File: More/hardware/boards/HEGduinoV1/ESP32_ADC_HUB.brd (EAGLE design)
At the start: 71.9 x 30 mm, 8 parts

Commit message: Added some sensor designs, moved some stuff
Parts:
- moved ADS1115 1.27 mm to (40.0, 38.5)
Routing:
- net ADC_GND: track 44.0 -> 45.4 mm
- net SDA: track 36.6 -> 37.9 mm
- net VBAT: track 89.8 -> 88.7 mm
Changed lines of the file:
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@@
 <attribute name="VALUE" x="55.047590625" y="28.01005" size="0.4064" layer="27" ratio="10" rot="R180"/>
 </element>
-<element name="ADS1115" library="microbuilder" package="1X10_ROUND70" value="" x="40.040815625" y="37.223853125" smashed="yes" rot="R180">
-<attribute name="NAME" x="27.298803125" y="39.482015625" size="0.8128" layer="26" ratio="10" rot="MR270"/>
-<attribute name="VALUE" x="52.740815625" y="40.398853125" size="0.8128" layer="27" rot="R180"/>
+<element name="ADS1115" library="microbuilder" package="1X10_ROUND70" value="" x="40.040815625" y="38.493853125" smashed="yes" rot="R180">
+<attribute name="NAME" x="27.298803125" y="40.752015625" size="0.8128" layer="26" ratio="10" rot="MR270"/>
+<attribute name="VALUE" x="52.740815625" y="41.668853125" size="0.8128" layer="27" rot="R180"/>
 </element>
 <element name="R1" library="resistor" library_urn="urn:adsk.eagle:library:348" package="0204/7" package3d_urn="urn:adsk.eagle:package:23498/1" value="" x="54.3327375" y="36.29111875" smashed="yes" rot="R270">
@@
 </signal>
 <signal name="VBAT">
-<wire x1="51.435" y1="40.005" x2="51.435" y2="37.1475" width="0.254" layer="1"/>
+<wire x1="51.435" y1="40.005" x2="51.435" y2="38.25875" width="0.254" layer="1"/>
 <wire x1="51.435" y1="40.005" x2="56.8325" y2="40.005" width="0.254" layer="1"/>
 <wire x1="51.435" y1="40.005" x2="19.52625" y2="40.005" width="0.254" layer="1"/>
@@
 <wire x1="50.165" y1="32.54375" x2="50.165" y2="41.43375" width="0.254" layer="16"/>
 <wire x1="50.165" y1="41.43375" x2="53.81625" y2="45.085" width="0.254" layer="16"/>
-<wire x1="43.815" y1="37.1475" x2="43.815" y2="32.54375" width="0.254" layer="16"/>
+<wire x1="43.815" y1="38.4175" x2="43.815" y2="32.54375" width="0.254" layer="16"/>
 <via x="43.815" y="32.54375" extent="1-16" drill="0.35"/>
 <wire x1="54.169665625" y1="32.534453125" x2="50.165" y2="32.54375" width="0" layer="19" extent="1-1"/>
-<wire x1="43.815" y1="32.54375" x2="41.062909375" y2="32.534453125" width="0" layer="19" extent="1-16"/>
+<wire x1="43.815" y1="32.54375" x2="41.062909375" y2="27.67456875" width="0" layer="19" extent="1-1"/>
 </signal>
 <signal name="SCL">
 <wire x1="46.51375" y1="31.115" x2="56.03875" y2="31.115" width="0.254" layer="16"/>
-<wire x1="46.51375" y1="39.21125" x2="46.51375" y2="33.3375" width="0.254" layer="16"/>
+<wire x1="46.51375" y1="39.0525" x2="46.51375" y2="33.3375" width="0.254" layer="16"/>
 <wire x1="46.51375" y1="33.3375" x2="43.65625" y2="30.48" width="0.254" layer="16"/>
 <wire x1="43.65625" y1="30.48" x2="43.65625" y2="27.6225" width="0.254" layer="16"/>
 <wire x1="46.51375" y1="33.3375" x2="46.51375" y2="31.115" width="0.254" layer="16"/>
-<wire x1="46.51375" y1="39.21125" x2="51.27625" y2="43.97375" width="0.254" layer="16"/>
-<wire x1="51.27625" y1="43.97375" x2="51.27625" y2="45.085" width="0.254" layer="16"/>
+<wire x1="46.51375" y1="39.0525" x2="51.27625" y2="43.815" width="0.254" layer="16"/>
+<wire x1="51.27625" y1="43.815" x2="51.27625" y2="45.085" width="0.254" layer="16"/>
 <wire x1="56.03875" y1="31.115" x2="56.8325" y2="31.90875" width="0.254" layer="16"/>
 <wire x1="56.8325" y1="31.90875" x2="56.8325" y2="32.385" width="0.254" layer="16"/>
@@
 </signal>
 <signal name="A0">
-<wire x1="40.9575" y1="42.06875" x2="36.195" y2="37.30625" width="0.508" layer="16"/>
+<wire x1="40.9575" y1="42.06875" x2="39.84625" y2="42.06875" width="0.508" layer="16"/>
+<wire x1="39.84625" y1="42.06875" x2="36.195" y2="38.4175" width="0.508" layer="16"/>
 <via x="40.9575" y="42.06875" extent="1-16" drill="0.3937"/>
 <wire x1="40.9575" y1="42.06875" x2="60.0075" y2="42.06875" width="0.508" layer="1"/>
@@
 <wire x1="24.60625" y1="26.035" x2="24.60625" y2="34.76625" width="0.254" layer="1"/>
 <wire x1="24.60625" y1="34.76625" x2="36.03625" y2="34.76625" width="0.254" layer="1"/>
-<wire x1="48.895" y1="34.76625" x2="48.895" y2="37.1475" width="0.254" layer="1"/>
+<wire x1="48.895" y1="34.76625" x2="48.895" y2="38.57625" width="0.254" layer="1"/>
 <wire x1="23.33625" y1="24.92375" x2="23.495" y2="24.92375" width="0.254" layer="1"/>
 <wire x1="23.495" y1="24.92375" x2="24.60625" y2="26.035" width="0.254" layer="1"/>

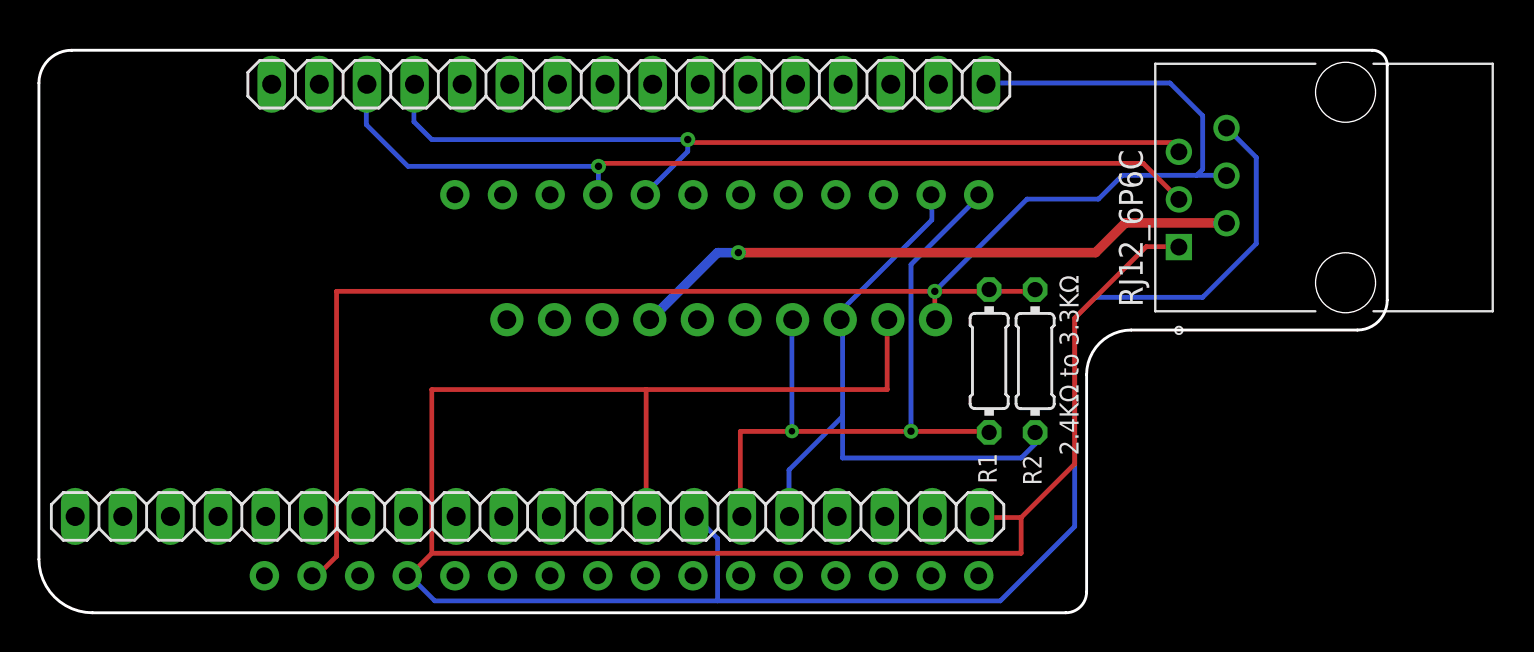
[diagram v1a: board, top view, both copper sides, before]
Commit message: updated HEG schematic (1.1, testing it)
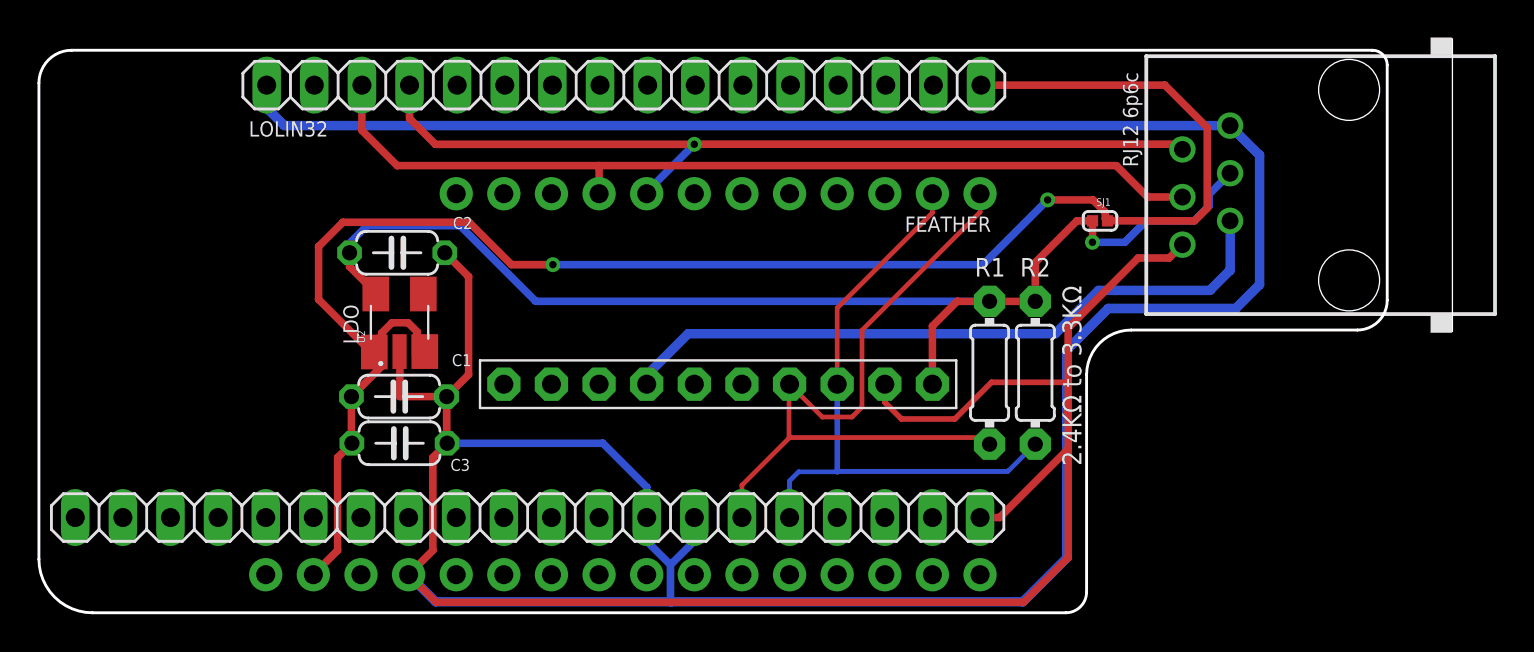
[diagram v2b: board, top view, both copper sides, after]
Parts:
- removed ADS1115: (no value), microbuilder:1X10_ROUND70
- removed HUZZAH32_A: (no value), microbuilder_merge:1X12_ROUND_MIN
- removed HUZZAH32_B: (no value), microbuilder_merge:1X16_ROUND_MIN
- removed LOLIN32_V1.0.0_A: (no value), pinhead:1X16
- removed LOLIN32_V1.0.0_B: (no value), pinhead:1X20
- removed RJ12_6P6C: (no value), A-2004-1-4-LP-N-R:ASSMANN_A-2004-1-4-LP-N-R
- added C1, C2: 1uF, rcl:C050-024X044
- added C3: 10uF, rcl:C050-024X044
- added J1: RJ11-2L-B, con-tycoelectronics:RJ11-NO_SHIELD
- added JP1: (no value), adafruit:1X12-CB
- added JP2: (no value), adafruit:1X15-CB
- added JP3: (no value), adafruit:1X01-CLEANBIG
- added JP4: (no value), pinhead:1X16
- added JP5: (no value), pinhead:1X20
- added SJ1: SOLDERJUMPERNC, headers:SJ_2S_SMALL
- added U1: PINHD-1X10, adafruit:1X10-BIG
- added U2: LP5907MFX-3.3/NOPB, LP5907MFX-3.3_NOPB:SOT95P280X145-5N
- R1, R2: value (none) -> 2.7k; device resistor:0204/7 -> adafruit:0204/7
- moved R1 0.63 mm to (54.4, 35.7)
- moved R2 0.63 mm to (56.8, 35.7)
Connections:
- new net A0: J1.2, U1.7
- new net GND: C1.2, C2.2, C3.2, J1.1, J1.6, JP2.4, JP4.1, JP5.13, JP5.14, JP5.20, U1.2, U2.2
- new net SCL: JP1.11, JP5.16, R2.2, U1.3
- new net SDA: JP1.12, JP5.15, R1.2, U1.4
- new net VANA: C2.1, J1.4, R1.1, R2.1, SJ1.2, U1.1, U2.5
- new net VBAT: C1.1, C3.1, JP2.2, JP4.16, SJ1.1, U2.1, U2.3
- new net VIR: J1.5, JP1.5, JP4.4
- new net VRED: J1.3, JP1.4, JP4.3
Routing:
- net GND: track 0.00 -> 242.4 mm
- net GND_DIG: track 72.2 -> 0.00 mm
- net VANA: track 0.00 -> 65.4 mm, vias 0 -> 1
- net GND_ANA: track 54.5 -> 0.00 mm
- net ADC_GND: track 45.4 -> 0.00 mm
- net VBAT: track 88.7 -> 93.2 mm, vias 1 -> 2
- net A0: track 33.1 -> 36.6 mm, vias 1 -> 0
- net SCL: track 34.0 -> 32.8 mm
- net VRED: track 48.5 -> 49.2 mm, vias 1 -> 0
- net SDA: track 37.9 -> 37.8 mm, vias 2 -> 0
- removed copper zone on layer 16, net BOT_COPPER
- removed copper zone on layer 1, net TOP_COPPER
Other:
- board text added: "ADS1115"
- board text added: "FEATHER"
- board text added: "LDO"
- board text added: "LOLIN32"
- board text added: "RJ12 6p6c"
- board text added: "v1.1 by Joshua Brewster"
- board text removed: "v1.0 by Joshua Brewster"
